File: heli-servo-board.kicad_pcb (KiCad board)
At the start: 2 copper layers, 24 x 24 mm, 12 parts, among them J1 Conn_01x06, J2 Conn_01x03, J3 Conn_01x03, J4 Conn_01x03, J6 Conn_01x02, J7 Conn_01x01, J8 Conn_01x01, J9 Conn_01x01

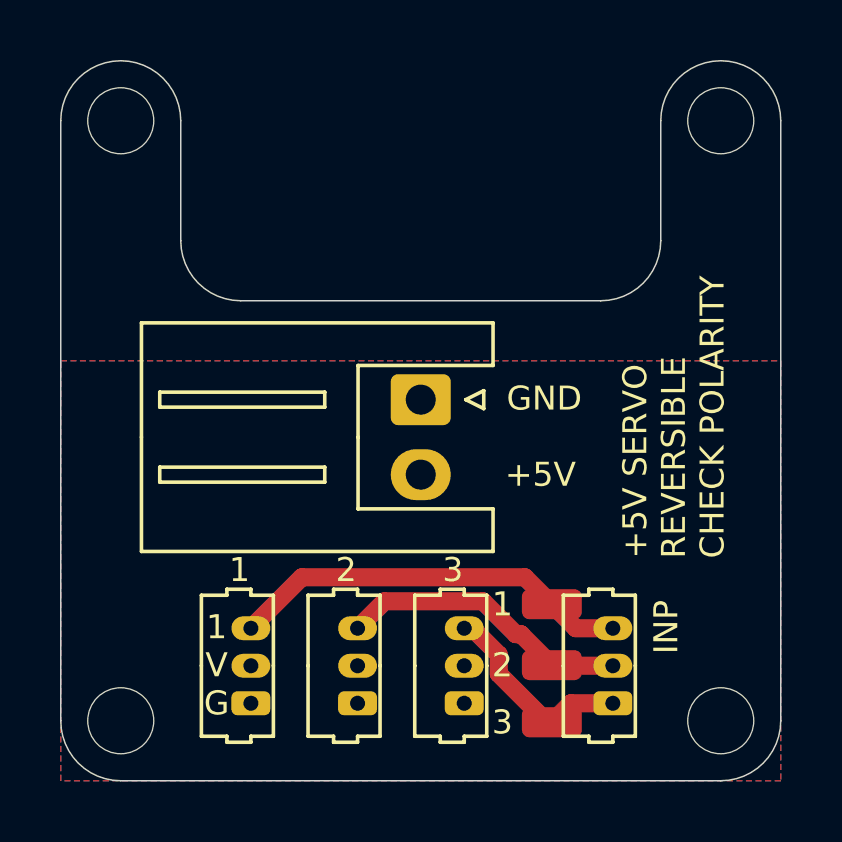
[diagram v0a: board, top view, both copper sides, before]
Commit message: Add 2.0mm power connectors.
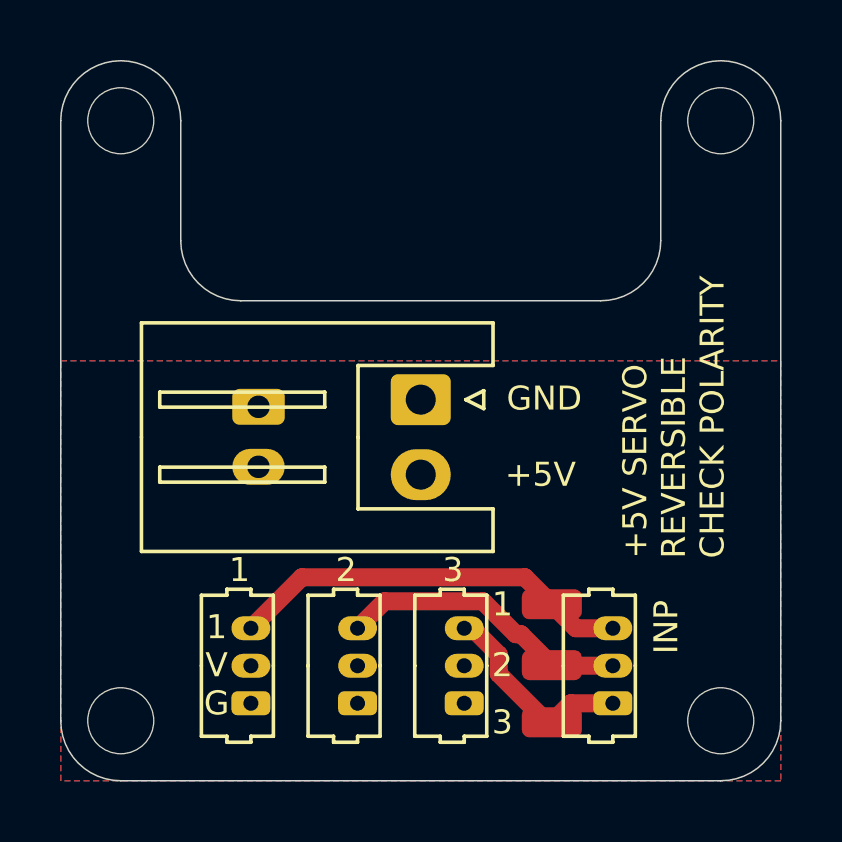
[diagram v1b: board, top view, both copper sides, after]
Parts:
- added REF**: JST_PH_B2B-PH-K_1x02_P2.00mm_Vertical, Connector_JST:JST_PH_B2B-PH-K_1x02_P2.00mm_Vertical, B.Cu at (164.6, 151.5)
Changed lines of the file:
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@@
     (tracks 19)
     (zones 0)
-    (modules 12)
+    (modules 13)
     (nets 6)
   )
@@
     (mod_text_size 1 1)
     (mod_text_width 0.15)
-    (pad_size 2.2 2.2)
-    (pad_drill 2.2)
+    (pad_size 1.2 1.75)
+    (pad_drill 0.75)
     (pad_to_mask_clearance 0)
     (aux_axis_origin 0 0)
@@
     (add_net "Net-(J1-Pad3)")
   )
+  (module Connector_JST:JST_PH_B2B-PH-K_1x02_P2.00mm_Vertical (layer B.Cu)
+    (at 164.592 151.5364 270)
+    (descr "JST PH series connector, B2B-PH-K (http://www.jst-mfg.com/product/pdf/eng/ePH.pdf), generated with kicad-footprint-generator")
+    (tags "connector JST PH side entry")
+    (fp_text reference REF** (at 1 2.9 270) (layer B.SilkS) hide
+      (effects (font (size 1 1) (thickness 0.15)) (justify mirror))
+    )
+    (fp_text value JST_PH_B2B-PH-K_1x02_P2.00mm_Vertical (at 1 -4 270) (layer B.Fab) hide
+      (effects (font (size 1 1) (thickness 0.15)) (justify mirror))
+    )
+    (fp_text user %R (at 1 -1.5 270) (layer B.Fab) hide
+      (effects (font (size 1 1) (thickness 0.15)) (justify mirror))
+    )
+    (fp_line (start -2.06 1.81) (end -2.06 -2.91) (layer B.SilkS) (width 0.12))
+    (fp_line (start -2.06 -2.91) (end 4.06 -2.91) (layer B.SilkS) (width 0.12))
+    (fp_line (start 4.06 -2.91) (end 4.06 1.81) (layer B.SilkS) (width 0.12))
+    (fp_line (start 4.06 1.81) (end -2.06 1.81) (layer B.SilkS) (width 0.12))
+    (fp_line (start -0.3 1.81) (end -0.3 2.01) (layer B.SilkS) (width 0.12))
+    (fp_line (start -0.3 2.01) (end -0.6 2.01) (layer B.SilkS) (width 0.12))
+    (fp_line (start -0.6 2.01) (end -0.6 1.81) (layer B.SilkS) (width 0.12))
+    (fp_line (start -0.3 1.91) (end -0.6 1.91) (layer B.SilkS) (width 0.12))
+    (fp_line (start 0.5 1.81) (end 0.5 1.2) (layer B.SilkS) (width 0.12))
+    (fp_line (start 0.5 1.2) (end -1.45 1.2) (layer B.SilkS) (width 0.12))
+    (fp_line (start -1.45 1.2) (end -1.45 -2.3) (layer B.SilkS) (width 0.12))
+    (fp_line (start -1.45 -2.3) (end 3.45 -2.3) (layer B.SilkS) (width 0.12))
+    (fp_line (start 3.45 -2.3) (end 3.45 1.2) (layer B.SilkS) (width 0.12))
+    (fp_line (start 3.45 1.2) (end 1.5 1.2) (layer B.SilkS) (width 0.12))
+    (fp_line (start 1.5 1.2) (end 1.5 1.81) (layer B.SilkS) (width 0.12))
+    (fp_line (start -2.06 0.5) (end -1.45 0.5) (layer B.SilkS) (width 0.12))
+    (fp_line (start -2.06 -0.8) (end -1.45 -0.8) (layer B.SilkS) (width 0.12))
+    (fp_line (start 4.06 0.5) (end 3.45 0.5) (layer B.SilkS) (width 0.12))
+    (fp_line (start 4.06 -0.8) (end 3.45 -0.8) (layer B.SilkS) (width 0.12))
+    (fp_line (start 0.9 -2.3) (end 0.9 -1.8) (layer B.SilkS) (width 0.12))
+    (fp_line (start 0.9 -1.8) (end 1.1 -1.8) (layer B.SilkS) (width 0.12))
+    (fp_line (start 1.1 -1.8) (end 1.1 -2.3) (layer B.SilkS) (width 0.12))
+    (fp_line (start 1 -2.3) (end 1 -1.8) (layer B.SilkS) (width 0.12))
+    (fp_line (start -1.11 2.11) (end -2.36 2.11) (layer B.SilkS) (width 0.12))
+    (fp_line (start -2.36 2.11) (end -2.36 0.86) (layer B.SilkS) (width 0.12))
+    (fp_line (start -1.11 2.11) (end -2.36 2.11) (layer B.Fab) (width 0.1))
+    (fp_line (start -2.36 2.11) (end -2.36 0.86) (layer B.Fab) (width 0.1))
+    (fp_line (start -1.95 1.7) (end -1.95 -2.8) (layer B.Fab) (width 0.1))
+    (fp_line (start -1.95 -2.8) (end 3.95 -2.8) (layer B.Fab) (width 0.1))
+    (fp_line (start 3.95 -2.8) (end 3.95 1.7) (layer B.Fab) (width 0.1))
+    (fp_line (start 3.95 1.7) (end -1.95 1.7) (layer B.Fab) (width 0.1))
+    (fp_line (start -2.45 2.2) (end -2.45 -3.3) (layer B.CrtYd) (width 0.05))
+    (fp_line (start -2.45 -3.3) (end 4.45 -3.3) (layer B.CrtYd) (width 0.05))
+    (fp_line (start 4.45 -3.3) (end 4.45 2.2) (layer B.CrtYd) (width 0.05))
+    (fp_line (start 4.45 2.2) (end -2.45 2.2) (layer B.CrtYd) (width 0.05))
+    (pad 2 thru_hole oval (at 2 0 270) (size 1.2 1.75) (drill 0.75) (layers *.Cu *.Mask)
+      (net 5 +BATT))
+    (pad 1 thru_hole roundrect (at 0 0 270) (size 1.2 1.75) (drill 0.75) (layers *.Cu *.Mask) (roundrect_rratio 0.208)
+      (net 4 GND))
+  )
   (module heli-servo-board:Molex_PicoBlade_53047-0310_1x03_P1.25mm_Vertical (layer F.Cu)

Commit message: The GHF13AIO is actually 16x16mm, redesigned with this mistake corrected
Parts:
- moved J7 5.34 mm to (173.3, 152.9)
- moved J8 5.34 mm to (173.3, 154.9)
- moved J9 5.34 mm to (173.3, 156.8)
- moved H3 4.00 mm to (176.0, 142.0)
- moved H4 4.00 mm to (176.0, 162.0)
- moved J1 3.97 mm to (175.9, 157.5)
- moved REF** 2.79 mm to (161.8, 151.5)
- moved J6 1.47 mm to (168.5, 151.3)
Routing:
- net Net-(J1-Pad3): track 13.5 -> 16.6 mm
- net Net-(J1-Pad2): track 9.77 -> 11.3 mm
- net Net-(J1-Pad1): track 6.89 -> 5.73 mm
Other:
- board size 24 x 24 mm -> 20 x 24 mm
- board text added: "+"
- board text added: "-"
- board text removed: "+5V SERVO REVERSIBLE CHECK POLARITY"
- board text removed: "G"
- board text removed: "V"

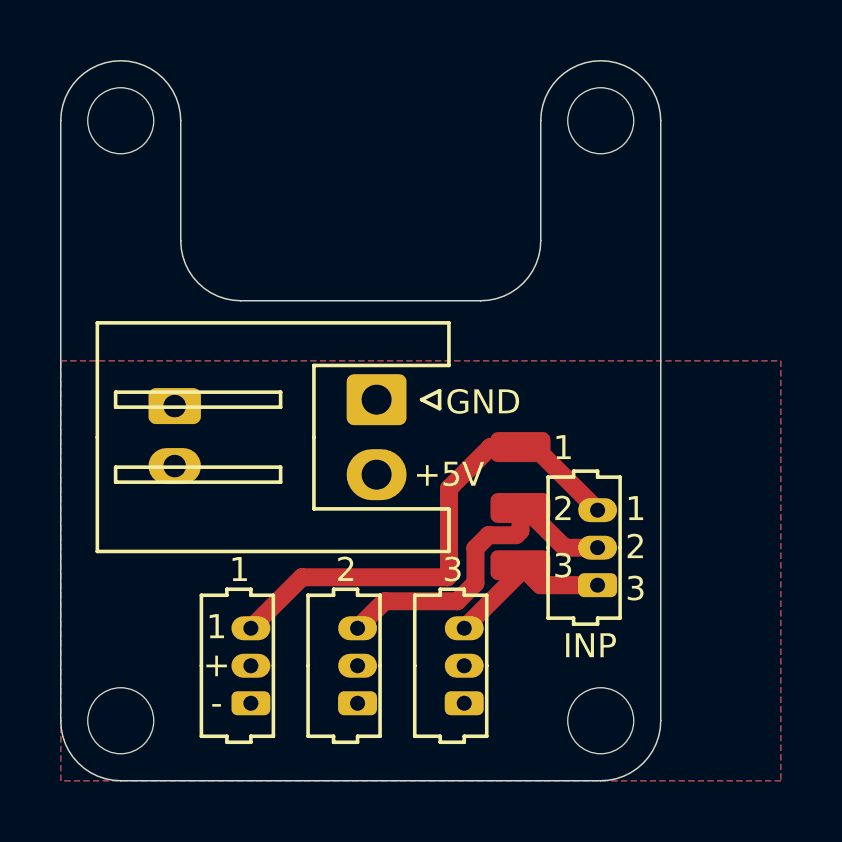
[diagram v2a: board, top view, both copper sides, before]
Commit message: Slightly adjust XH horizontal position.
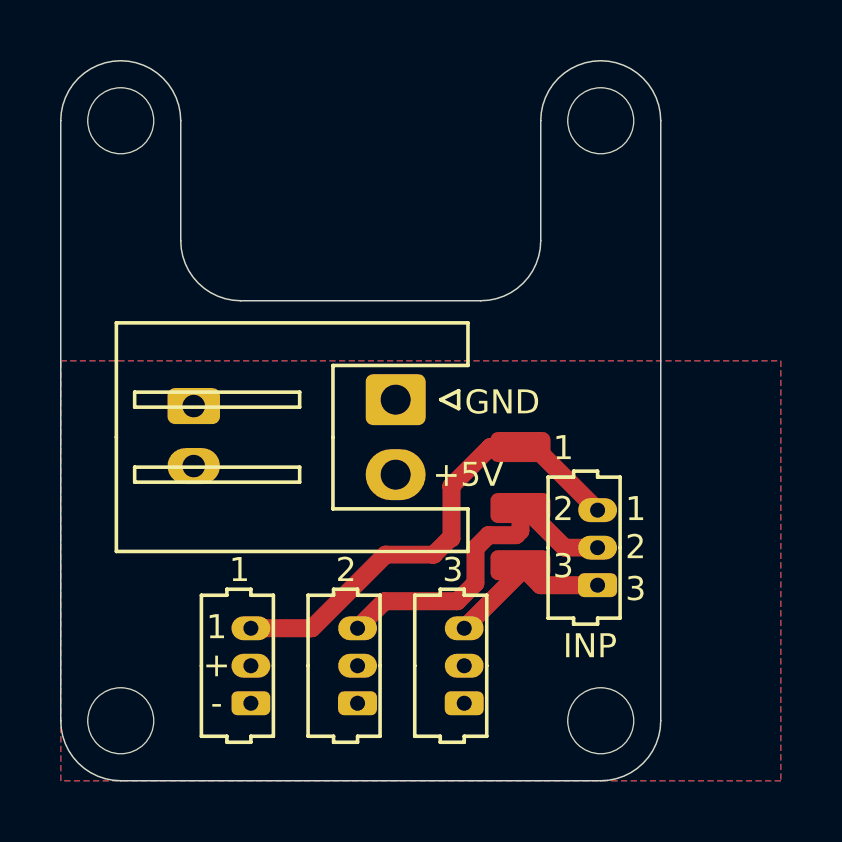
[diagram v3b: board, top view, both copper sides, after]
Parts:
- moved J6 0.63 mm to (169.2, 151.3)
- moved REF** 0.63 mm to (162.4, 151.5)
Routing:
- net Net-(J1-Pad3): track 16.6 -> 16.0 mm
